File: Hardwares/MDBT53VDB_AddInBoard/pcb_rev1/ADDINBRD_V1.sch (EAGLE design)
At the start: 21 parts, among them CN1 51296-0894, CN2 IF_6PIN, CN3 IF_3PIN, CN4 IF_4PIN, Q1 BSS84AKQBZ, U1 RV-3028-C7

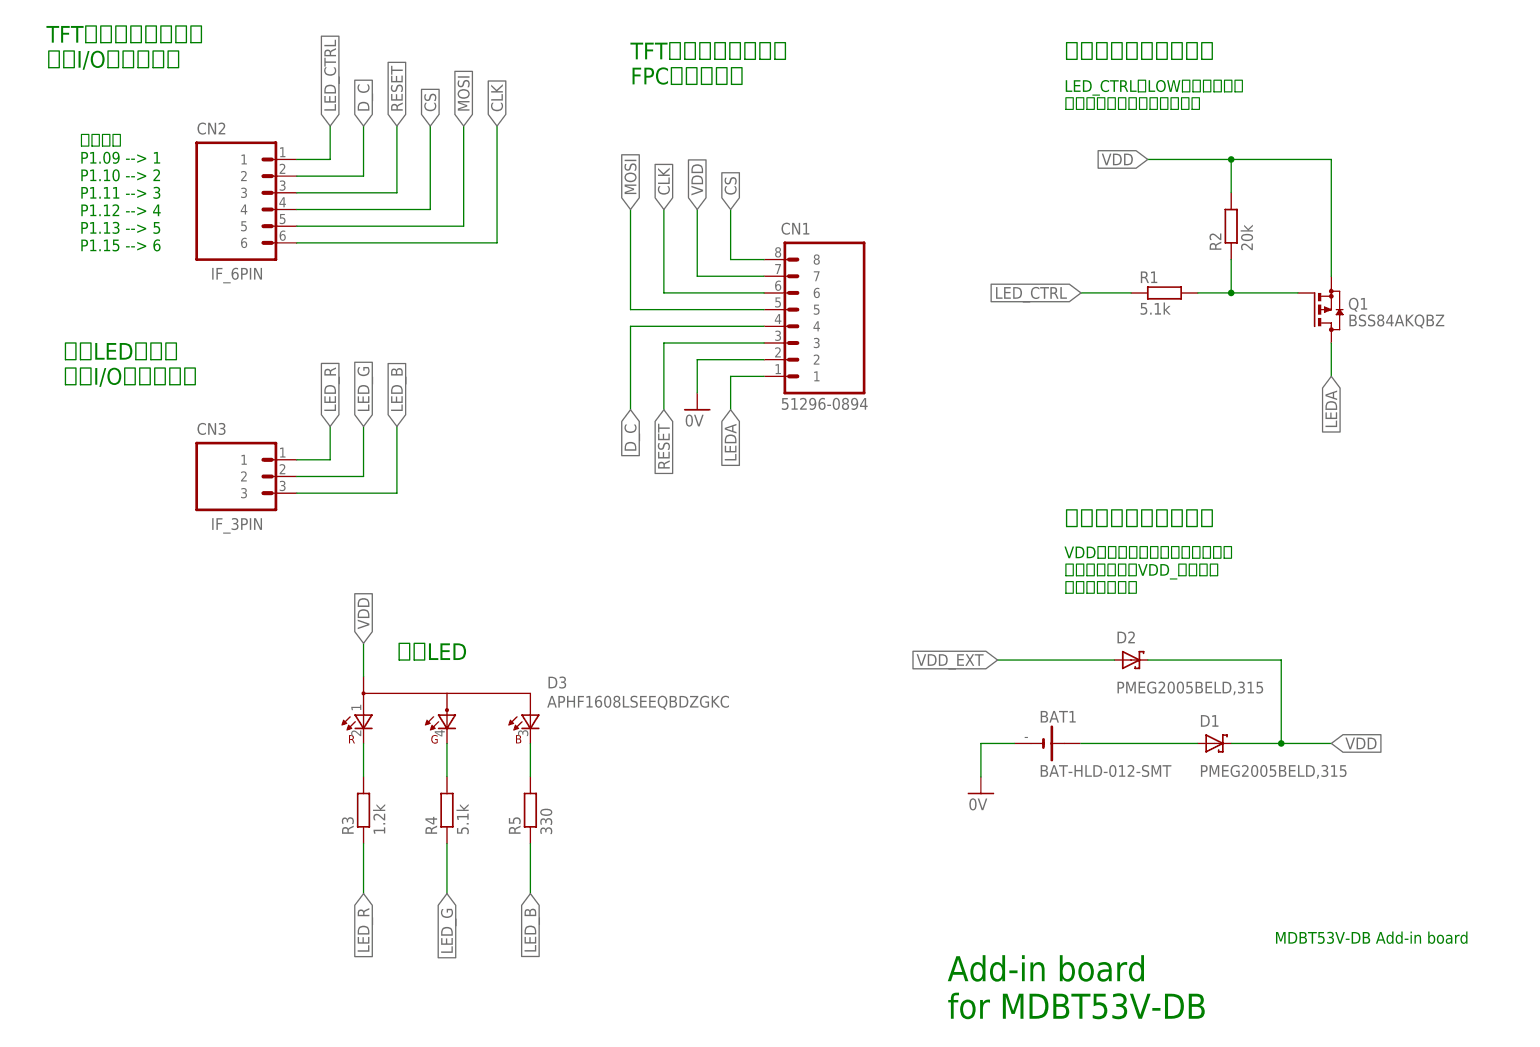
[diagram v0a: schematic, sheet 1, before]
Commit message: 回路図を修正
・ERCを通す
・ボタン乾電池とVDDの間に、2pinジャンパーヘッダーを設置
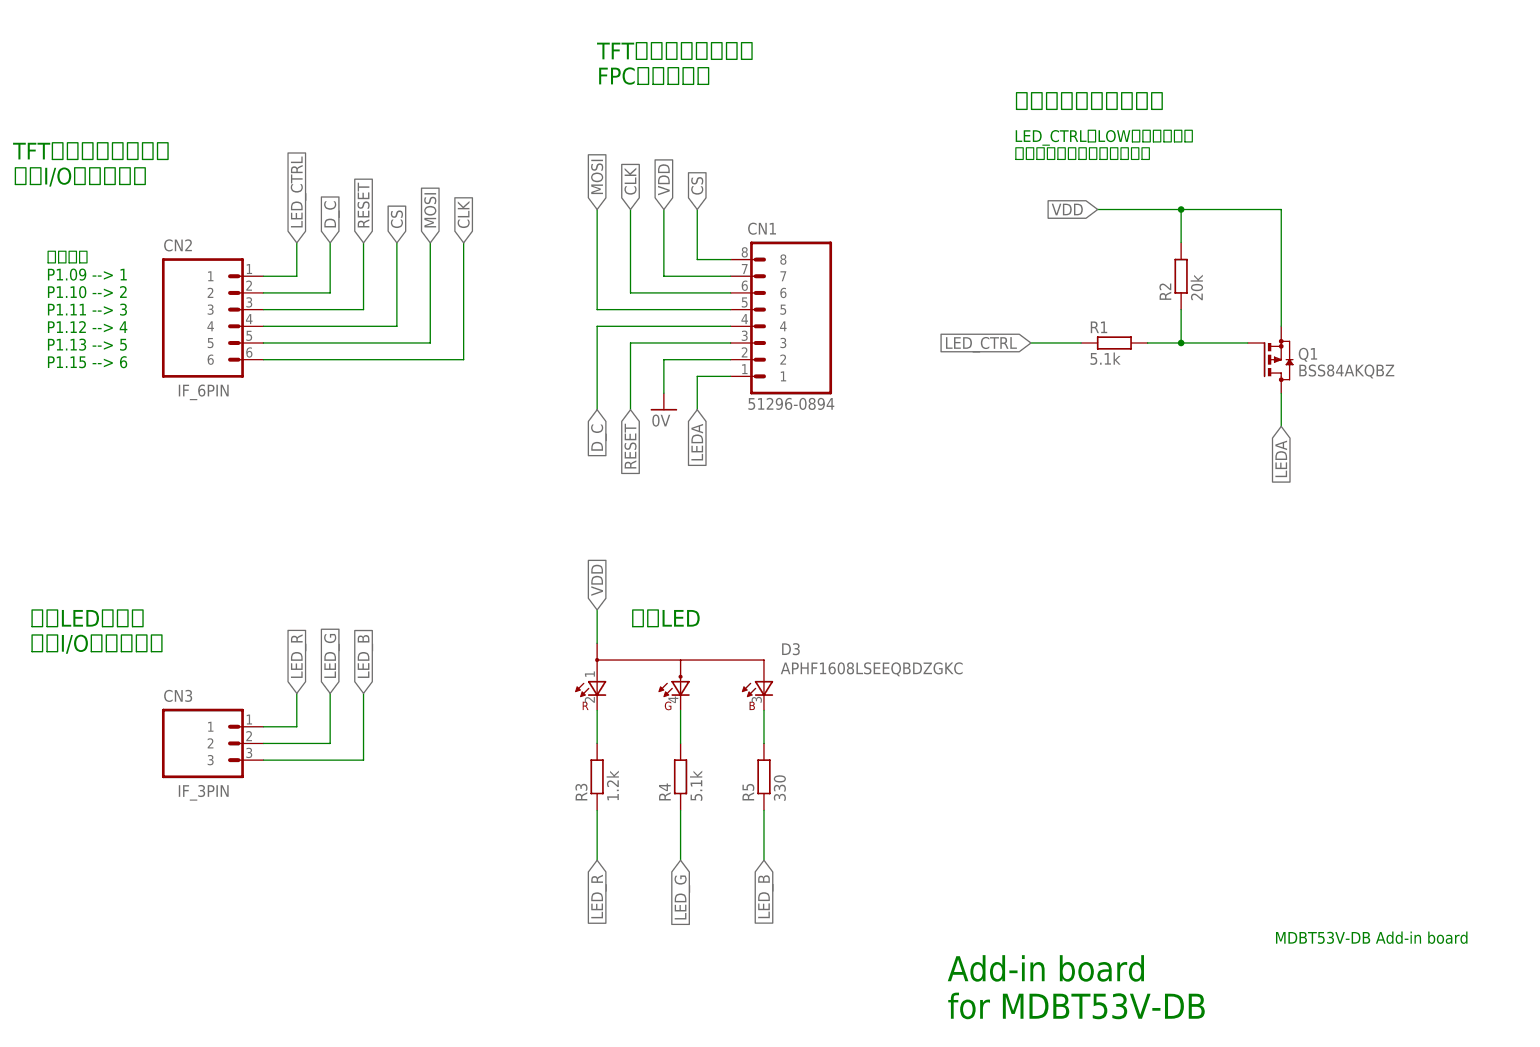
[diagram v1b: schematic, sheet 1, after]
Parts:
- removed BAT1: BAT-HLD-012-SMT, Connectors:BAT-HLD-012-SMT
- added BAT2: BAT-HLD-012-SMT, Connectors:BAT-HLD-012-SMT
- added CN5: IF_2PIN_H, Connectors:IF_2PIN_H
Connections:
- net 0V: now also BAT2.-; no longer BAT1.-
- net N$2: now also CN5.1, D1.C; no longer BAT1.+, D1.A
- net VDD: now also CN5.2; no longer D1.C
- net VDD_BATT: now also BAT2.+, D1.A
- net VDD_EXT: now also CN4.4
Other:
- note added: "ピン対応 VDD_BATT --> 1 VDD --> 2"
- note added: "ボタン電池からの 電源供給切り替え"
- note removed: "電源回路（要：検討）"
- moved on the sheet: C1, C2, CN1, CN2, CN3, CN4, D3, Q1, R1, R2, R3, R4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

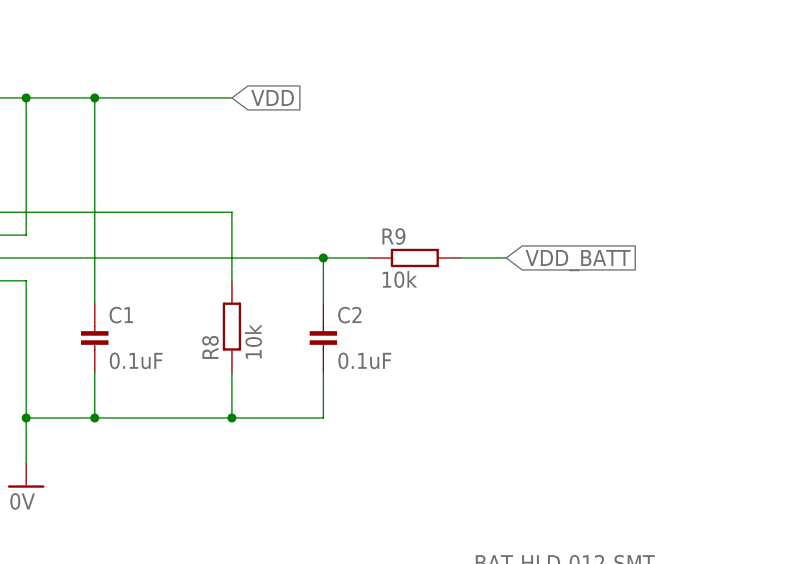
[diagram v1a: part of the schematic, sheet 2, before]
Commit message: 回路図を修正
・定数を修正
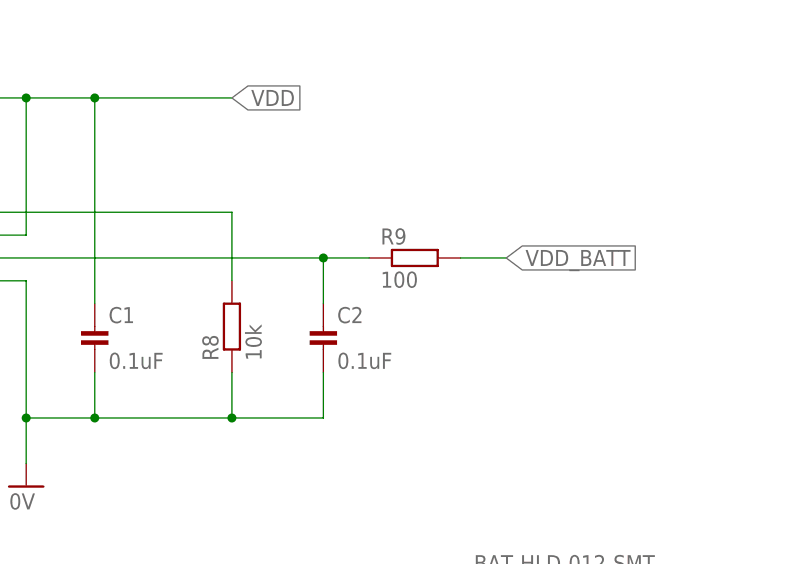
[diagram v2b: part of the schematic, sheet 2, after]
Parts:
- R9: value 10k -> 100
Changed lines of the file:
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@@
 <part name="R5" library="Parts" deviceset="RESISTOR" device="_0402N" value="330"/>
 <part name="C2" library="Parts" deviceset="CAP" device="_0402N" value="0.1uF"/>
-<part name="R9" library="Parts" deviceset="RESISTOR" device="_0402N" value="10k"/>
+<part name="R9" library="Parts" deviceset="RESISTOR" device="_0402N" value="100"/>
 <part name="CN5" library="Connectors" deviceset="IF_2PIN" device="_H"/>
 <part name="BAT2" library="Connectors" deviceset="BAT-HLD-012-SMT" device=""/>

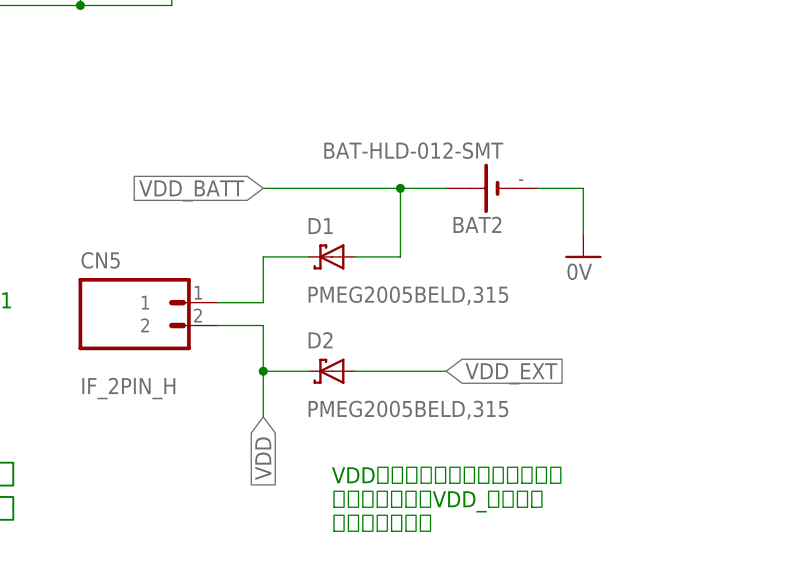
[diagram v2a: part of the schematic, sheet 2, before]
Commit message: 回路図を修正
・部品番号を修正
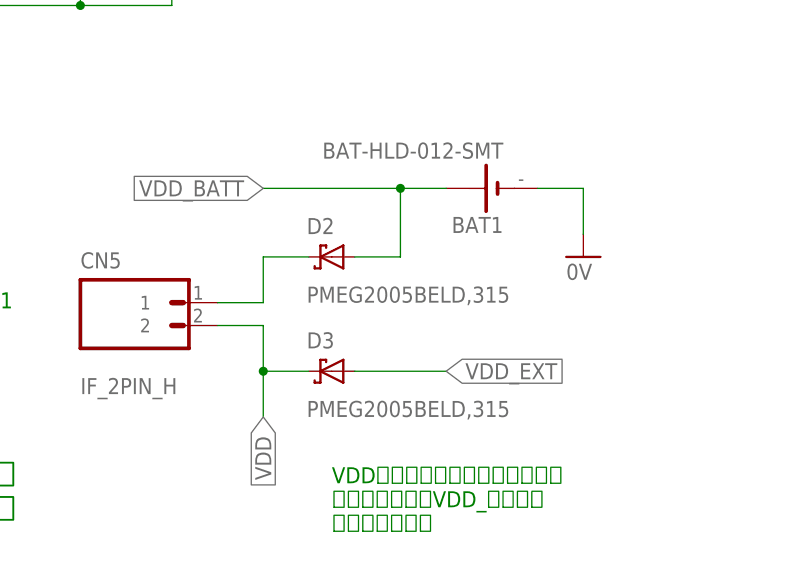
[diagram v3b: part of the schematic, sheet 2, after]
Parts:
- D1: value PMEG2005BELD,315 -> APHF1608LSEEQBDZGKC; device Parts:PMEG2005BELD,315 -> Parts:APHF1608LSEEQBDZGKC
- D3: value APHF1608LSEEQBDZGKC -> PMEG2005BELD,315; device Parts:APHF1608LSEEQBDZGKC -> Parts:PMEG2005BELD,315
- renumbered BAT2 to BAT1
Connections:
- net N$10: now also D1.CBLUE; no longer D3.CBLUE
- net N$2: now also D2.C; no longer D1.C
- net N$5: now also D1.CGREEN; no longer D3.CGREEN
- net N$6: now also D1.CRED; no longer D3.CRED
- net VDD: now also D1.A, D3.C; no longer D2.C, D3.A
- net VDD_BATT: now also D2.A; no longer D1.A
- net VDD_EXT: now also D3.A; no longer D2.A
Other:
- moved on the sheet: D2
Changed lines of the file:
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@@
 <part name="C1" library="Parts" deviceset="CAP" device="_0402N" value="0.1uF"/>
 <part name="CN3" library="Connectors" deviceset="IF_3PIN" device=""/>
-<part name="D3" library="Parts" deviceset="APHF1608" device="LSEEQBDZGKC"/>
+<part name="D1" library="Parts" deviceset="APHF1608" device="LSEEQBDZGKC"/>
 <part name="R3" library="Parts" deviceset="RESISTOR" device="_0402N" value="1.2k"/>
 <part name="R4" library="Parts" deviceset="RESISTOR" device="_0402N" value="5.1k"/>
@@
 <part name="R9" library="Parts" deviceset="RESISTOR" device="_0402N" value="100"/>
 <part name="CN5" library="Connectors" deviceset="IF_2PIN" device="_H"/>
-<part name="BAT2" library="Connectors" deviceset="BAT-HLD-012-SMT" device=""/>
+<part name="BAT1" library="Connectors" deviceset="BAT-HLD-012-SMT" device=""/>
 <part name="GND5" library="Supply" deviceset="0V" device=""/>
-<part name="D1" library="Parts" deviceset="PMEG2005" device="BELD,315"/>
 <part name="D2" library="Parts" deviceset="PMEG2005" device="BELD,315"/>
+<part name="D3" library="Parts" deviceset="PMEG2005" device="BELD,315"/>
 </parts>
 <sheets>
@@
 <attribute name="NAME" x="48.26" y="57.15" size="1.778" layer="95"/>
 </instance>
-<instance part="D3" gate="G$1" x="127" y="60.96"/>
+<instance part="D1" gate="G$1" x="127" y="60.96"/>
 <instance part="R3" gate="G$1" x="114.3" y="40.64" rot="R90"/>
 <instance part="R4" gate="G$1" x="127" y="40.64" rot="R90"/>
@@
 </segment>
 <segment>
-<pinref part="D3" gate="G$1" pin="A"/>
+<pinref part="D1" gate="G$1" pin="A"/>
 <wire x1="114.3" y1="66.04" x2="114.3" y2="71.12" width="0.1524" layer="91"/>
 <label x="114.3" y="71.12" size="1.778" layer="95" rot="R90" xref="yes"/>
@@
 <net name="N$6" class="0">
 <segment>
-<pinref part="D3" gate="G$1" pin="CRED"/>
+<pinref part="D1" gate="G$1" pin="CRED"/>
 <pinref part="R3" gate="G$1" pin="2"/>
 <wire x1="114.3" y1="55.88" x2="114.3" y2="50.8" width="0.1524" layer="91"/>
@@
 <net name="N$10" class="0">
 <segment>
-<pinref part="D3" gate="G$1" pin="CBLUE"/>
+<pinref part="D1" gate="G$1" pin="CBLUE"/>
 <pinref part="R5" gate="G$1" pin="2"/>
 <wire x1="139.7" y1="55.88" x2="139.7" y2="50.8" width="0.1524" layer="91"/>
@@
 <net name="N$5" class="0">
 <segment>
-<pinref part="D3" gate="G$1" pin="CGREEN"/>
+<pinref part="D1" gate="G$1" pin="CGREEN"/>
 <pinref part="R4" gate="G$1" pin="2"/>
 <wire x1="127" y1="55.88" x2="127" y2="50.8" width="0.1524" layer="91"/>
@@
 <attribute name="NAME" x="152.4" y="74.93" size="1.778" layer="95"/>
 </instance>
-<instance part="BAT2" gate="G$1" x="198.12" y="83.82" rot="R180"/>
+<instance part="BAT1" gate="G$1" x="198.12" y="83.82" rot="R180"/>
 <instance part="GND5" gate="1" x="208.28" y="76.2"/>
-<instance part="D1" gate="G$1" x="180.34" y="76.2" smashed="yes" rot="R180">
+<instance part="D2" gate="G$1" x="180.34" y="76.2" smashed="yes" rot="R180">
 <attribute name="NAME" x="177.546" y="78.74" size="1.778" layer="95"/>
 <attribute name="VALUE" x="177.546" y="71.12" size="1.778" layer="96"/>
 </instance>
-<instance part="D2" gate="G$1" x="180.34" y="63.5" smashed="yes" rot="R180">
+<instance part="D3" gate="G$1" x="180.34" y="63.5" smashed="yes" rot="R180">
 <attribute name="NAME" x="177.546" y="66.04" size="1.778" layer="95"/>
 <attribute name="VALUE" x="177.546" y="58.42" size="1.778" layer="96"/>
@@
 </segment>
 <segment>
-<pinref part="BAT2" gate="G$1" pin="-"/>
+<pinref part="BAT1" gate="G$1" pin="-"/>
 <pinref part="GND5" gate="1" pin="0V"/>
 <wire x1="203.2" y1="83.82" x2="208.28" y2="83.82" width="0.1524" layer="91"/>
@@
 <wire x1="172.72" y1="68.58" x2="172.72" y2="63.5" width="0.1524" layer="91"/>
 <label x="172.72" y="58.42" size="1.778" layer="95" rot="R270" xref="yes"/>
-<pinref part="D2" gate="G$1" pin="C"/>
+<pinref part="D3" gate="G$1" pin="C"/>
 <wire x1="172.72" y1="63.5" x2="172.72" y2="58.42" width="0.1524" layer="91"/>
 <wire x1="177.8" y1="63.5" x2="172.72" y2="63.5" width="0.1524" layer="91"/>
@@
 </segment>
 <segment>
-<pinref part="BAT2" gate="G$1" pin="+"/>
+<pinref part="BAT1" gate="G$1" pin="+"/>
 <wire x1="193.04" y1="83.82" x2="187.96" y2="83.82" width="0.1524" layer="91"/>
 <label x="172.72" y="83.82" size="1.778" layer="95" rot="R180" xref="yes"/>
 <junction x="187.96" y="83.82"/>
 <wire x1="187.96" y1="83.82" x2="172.72" y2="83.82" width="0.1524" layer="91"/>
-<pinref part="D1" gate="G$1" pin="A"/>
+<pinref part="D2" gate="G$1" pin="A"/>
 <wire x1="182.88" y1="76.2" x2="187.96" y2="76.2" width="0.1524" layer="91"/>
 <wire x1="187.96" y1="76.2" x2="187.96" y2="83.82" width="0.1524" layer="91"/>
@@
 <wire x1="167.64" y1="71.12" x2="172.72" y2="71.12" width="0.1524" layer="91"/>
 <wire x1="172.72" y1="71.12" x2="172.72" y2="76.2" width="0.1524" layer="91"/>
-<pinref part="D1" gate="G$1" pin="C"/>
+<pinref part="D2" gate="G$1" pin="C"/>
 <wire x1="172.72" y1="76.2" x2="177.8" y2="76.2" width="0.1524" layer="91"/>
 </segment>
@@
 </segment>
 <segment>
-<pinref part="D2" gate="G$1" pin="A"/>
+<pinref part="D3" gate="G$1" pin="A"/>
 <wire x1="182.88" y1="63.5" x2="193.04" y2="63.5" width="0.1524" layer="91"/>
 <label x="193.04" y="63.5" size="1.778" layer="95" xref="yes"/>
